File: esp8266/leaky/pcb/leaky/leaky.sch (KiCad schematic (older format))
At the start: 31 parts, among them J1 UART, J2 extra pins, Q1 BC327, SW1 sensing top, SW2 sensing bot, U1 DD0405MA, U2 ESP-12F

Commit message: leaky: Test routing
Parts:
- removed SW2: sensing bot, Connector_PinHeader_2.54mm:PinHeader_1x02_P2.54mm_Vertical, symbol Switch:SW_SPST
- SW1: value sensing top -> sensing loop
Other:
- moved on the sheet: C3, JP2, Q1, R1, R2, R3, SW1, TP3, TP4
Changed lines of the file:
@@
 L Transistor_BJT:BC327 Q1
 U 1 1 5F78C4AB
-P 2050 2350
-F 0 "Q1" H 2241 2304 50  0000 L CNN
-F 1 "BC327" H 2241 2395 50  0000 L CNN
-F 2 "Package_TO_SOT_THT:TO-92_Inline" H 2250 2275 50  0001 L CIN
-F 3 "http://www.onsemi.com/pub_link/Collateral/BC327-D.PDF" H 2050 2350 50  0001 L CNN
-	1    2050 2350
+P 1910 2640
+F 0 "Q1" H 2101 2594 50  0000 L CNN
+F 1 "BC327" H 2101 2685 50  0000 L CNN
+F 2 "Package_TO_SOT_THT:TO-92_Inline" H 2110 2565 50  0001 L CIN
+F 3 "http://www.onsemi.com/pub_link/Collateral/BC327-D.PDF" H 1910 2640 50  0001 L CNN
+	1    1910 2640
 	1    0    0    1
 $EndComp
@@
 L power:+3V3 #PWR0105
 U 1 1 5F78E830
-P 2150 2150
-F 0 "#PWR0105" H 2150 2000 50  0001 C CNN
-F 1 "+3V3" H 2165 2323 50  0000 C CNN
-F 2 "" H 2150 2150 50  0001 C CNN
-F 3 "" H 2150 2150 50  0001 C CNN
-	1    2150 2150
+P 2010 2440
+F 0 "#PWR0105" H 2010 2290 50  0001 C CNN
+F 1 "+3V3" H 2025 2613 50  0000 C CNN
+F 2 "" H 2010 2440 50  0001 C CNN
+F 3 "" H 2010 2440 50  0001 C CNN
+	1    2010 2440
 	1    0    0    -1
 $EndComp
@@
 L Device:R_Small R1
 U 1 1 5F78FD80
-P 1750 2350
-F 0 "R1" V 1650 2350 50  0000 C CNN
-F 1 "1k" V 1850 2350 50  0000 C CNN
-F 2 "Resistor_SMD:R_0805_2012Metric_Pad1.15x1.40mm_HandSolder" H 1750 2350 50  0001 C CNN
-F 3 "~" H 1750 2350 50  0001 C CNN
-	1    1750 2350
+P 1610 2640
+F 0 "R1" V 1510 2640 50  0000 C CNN
+F 1 "1k" V 1710 2640 50  0000 C CNN
+F 2 "Resistor_SMD:R_0805_2012Metric_Pad1.15x1.40mm_HandSolder" H 1610 2640 50  0001 C CNN
+F 3 "~" H 1610 2640 50  0001 C CNN
+	1    1610 2640
 	0    1    1    0
 $EndComp
@@
 L Switch:SW_SPST SW1
 U 1 1 5F792B65
-P 1100 2350
-F 0 "SW1" H 950 2450 50  0000 C CNN
-F 1 "sensing top" H 1150 2250 50  0000 C CNN
-F 2 "Connector_PinHeader_2.54mm:PinHeader_1x02_P2.54mm_Vertical" H 1100 2350 50  0001 C CNN
-F 3 "~" H 1100 2350 50  0001 C CNN
-	1    1100 2350
+P 1180 2640
+F 0 "SW1" H 1030 2740 50  0000 C CNN
+F 1 "sensing loop" H 1140 2540 50  0000 C CNN
+F 2 "Connector_PinHeader_2.54mm:PinHeader_1x02_P2.54mm_Vertical" H 1180 2640 50  0001 C CNN
+F 3 "~" H 1180 2640 50  0001 C CNN
+	1    1180 2640
 	-1   0    0    -1
 $EndComp
@@
 L power:GND #PWR01
 U 1 1 5F793765
-P 800 3080
-F 0 "#PWR01" H 800 2830 50  0001 C CNN
-F 1 "GND" H 805 2907 50  0000 C CNN
-F 2 "" H 800 3080 50  0001 C CNN
-F 3 "" H 800 3080 50  0001 C CNN
-	1    800  3080
+P 860 2820
+F 0 "#PWR01" H 860 2570 50  0001 C CNN
+F 1 "GND" H 865 2647 50  0000 C CNN
+F 2 "" H 860 2820 50  0001 C CNN
+F 3 "" H 860 2820 50  0001 C CNN
+	1    860  2820
 	1    0    0    -1
 $EndComp
@@
 L Device:R_Small R2
 U 1 1 5F7959A8
-P 2150 3000
-F 0 "R2" H 1950 3050 50  0000 L CNN
-F 1 "1k" H 1950 2950 50  0000 L CNN
-F 2 "Resistor_SMD:R_0805_2012Metric_Pad1.15x1.40mm_HandSolder" H 2150 3000 50  0001 C CNN
-F 3 "~" H 2150 3000 50  0001 C CNN
-	1    2150 3000
+P 2010 3290
+F 0 "R2" H 1810 3340 50  0000 L CNN
+F 1 "1k" H 1810 3240 50  0000 L CNN
+F 2 "Resistor_SMD:R_0805_2012Metric_Pad1.15x1.40mm_HandSolder" H 2010 3290 50  0001 C CNN
+F 3 "~" H 2010 3290 50  0001 C CNN
+	1    2010 3290
 	1    0    0    -1
 $EndComp
@@
 L power:GND #PWR02
 U 1 1 5F7965D3
-P 2150 3200
-F 0 "#PWR02" H 2150 2950 50  0001 C CNN
-F 1 "GND" H 2155 3027 50  0000 C CNN
-F 2 "" H 2150 3200 50  0001 C CNN
-F 3 "" H 2150 3200 50  0001 C CNN
-	1    2150 3200
-	1    0    0    -1
-$EndComp
-Wire Wire Line
-	2150 3200 2150 3150
+P 2010 3490
+F 0 "#PWR02" H 2010 3240 50  0001 C CNN
+F 1 "GND" H 2015 3317 50  0000 C CNN
+F 2 "" H 2010 3490 50  0001 C CNN
+F 3 "" H 2010 3490 50  0001 C CNN
+	1    2010 3490
+	1    0    0    -1
+$EndComp
+Wire Wire Line
+	2010 3490 2010 3440
 $Comp
 L Device:R_Small R3
 U 1 1 5F796B46
-P 2450 2850
-F 0 "R3" V 2350 2800 50  0000 L CNN
-F 1 "10k" V 2550 2800 50  0000 L CNN
-F 2 "Resistor_SMD:R_0805_2012Metric_Pad1.15x1.40mm_HandSolder" H 2450 2850 50  0001 C CNN
-F 3 "~" H 2450 2850 50  0001 C CNN
-	1    2450 2850
-	0    1    1    0
-$EndComp
-Wire Wire Line
-	2350 2850 2150 2850
-Connection ~ 2150 2850
-Wire Wire Line
-	2150 2850 2150 2900
+P 2310 3140
+F 0 "R3" V 2210 3090 50  0000 L CNN
+F 1 "10k" V 2410 3090 50  0000 L CNN
+F 2 "Resistor_SMD:R_0805_2012Metric_Pad1.15x1.40mm_HandSolder" H 2310 3140 50  0001 C CNN
+F 3 "~" H 2310 3140 50  0001 C CNN
+	1    2310 3140
+	0    1    1    0
+$EndComp
+Wire Wire Line
+	2210 3140 2010 3140
+Connection ~ 2010 3140
+Wire Wire Line
+	2010 3140 2010 3190
 $Comp
 L Device:C_Small C3
 U 1 1 5F797694
-P 2700 2950
-F 0 "C3" H 2850 2950 50  0000 C CNN
-F 1 "10uF" H 2850 2850 50  0000 C CNN
-F 2 "Capacitor_SMD:C_0805_2012Metric_Pad1.18x1.45mm_HandSolder" H 2700 2950 50  0001 C CNN
-F 3 "~" H 2700 2950 50  0001 C CNN
-	1    2700 2950
-	1    0    0    -1
-$EndComp
-Wire Wire Line
-	2550 2850 2700 2850
-Connection ~ 2150 3150
-Wire Wire Line
-	2150 3150 2150 3100
-Text GLabel 3050 2850 2    50   Input ~ 0
+P 2560 3240
+F 0 "C3" H 2710 3240 50  0000 C CNN
+F 1 "10uF" H 2710 3140 50  0000 C CNN
+F 2 "Capacitor_SMD:C_0805_2012Metric_Pad1.18x1.45mm_HandSolder" H 2560 3240 50  0001 C CNN
+F 3 "~" H 2560 3240 50  0001 C CNN
+	1    2560 3240
+	1    0    0    -1
+$EndComp
+Wire Wire Line
+	2410 3140 2560 3140
+Connection ~ 2010 3440
+Wire Wire Line
+	2010 3440 2010 3390
+Text GLabel 2910 3140 2    50   Input ~ 0
 EN
-Connection ~ 2700 2850
-Wire Wire Line
-	2700 3050 2700 3150
-Wire Wire Line
-	2700 2850 2900 2850
-Wire Wire Line
-	2700 3150 2150 3150
-Wire Wire Line
-	1300 2350 1450 2350
-Wire Wire Line
-	1450 2700 1300 2700
-Connection ~ 1450 2350
-Wire Wire Line
-	1450 2350 1650 2350
-Wire Wire Line
-	900  2350 800  2350
-Wire Wire Line
-	800  2350 800  2700
-Wire Wire Line
-	800  2700 900  2700
-Connection ~ 800  2700
+Connection ~ 2560 3140
+Wire Wire Line
+	2560 3340 2560 3440
+Wire Wire Line
+	2560 3140 2760 3140
+Wire Wire Line
+	2560 3440 2010 3440
 $Comp
 L power:+3V3 #PWR07
@@
 L Device:Jumper_NO_Small JP2
 U 1 1 5F7E84A9
-P 2700 2550
-F 0 "JP2" V 2700 2350 50  0000 L CNN
-F 1 "TURN_ON" V 2700 2600 50  0000 L CNN
-F 2 "Connector_PinHeader_2.54mm:PinHeader_1x02_P2.54mm_Vertical" H 2700 2550 50  0001 C CNN
-F 3 "~" H 2700 2550 50  0001 C CNN
-	1    2700 2550
+P 2560 2840
+F 0 "JP2" V 2560 2640 50  0000 L CNN
+F 1 "TURN_ON" V 2560 2890 50  0000 L CNN
+F 2 "Connector_PinHeader_2.54mm:PinHeader_1x02_P2.54mm_Vertical" H 2560 2840 50  0001 C CNN
+F 3 "~" H 2560 2840 50  0001 C CNN
+	1    2560 2840
 	0    1    1    0
 $EndComp
@@
 $EndComp
 Wire Wire Line
-	2700 2650 2150 2650
-Wire Wire Line
-	2150 2650 2150 2550
-Wire Wire Line
-	2150 2650 2150 2750
-Connection ~ 2150 2650
-Wire Wire Line
-	2700 2150 2700 2450
+	2560 2940 2010 2940
+Wire Wire Line
+	2010 2940 2010 2840
+Wire Wire Line
+	2010 2940 2010 3040
+Connection ~ 2010 2940
+Wire Wire Line
+	2560 2440 2560 2740
 $Comp
 L power:+3V3 #PWR011
 U 1 1 5F7EE7D8
-P 2700 2150
-F 0 "#PWR011" H 2700 2000 50  0001 C CNN
-F 1 "+3V3" H 2715 2323 50  0000 C CNN
-F 2 "" H 2700 2150 50  0001 C CNN
-F 3 "" H 2700 2150 50  0001 C CNN
-	1    2700 2150
+P 2560 2440
+F 0 "#PWR011" H 2560 2290 50  0001 C CNN
+F 1 "+3V3" H 2575 2613 50  0000 C CNN
+F 2 "" H 2560 2440 50  0001 C CNN
+F 3 "" H 2560 2440 50  0001 C CNN
+	1    2560 2440
 	1    0    0    -1
 $EndComp
@@
 L Connector:TestPoint TP4
 U 1 1 5F7F5357
-P 2900 2850
-F 0 "TP4" H 2950 3000 50  0000 L CNN
-F 1 "TestPoint" H 2958 2877 50  0001 L CNN
-F 2 "TestPoint:TestPoint_Pad_D1.0mm" H 3100 2850 50  0001 C CNN
-F 3 "~" H 3100 2850 50  0001 C CNN
-	1    2900 2850
-	1    0    0    -1
-$EndComp
-Connection ~ 2900 2850
-Wire Wire Line
-	2900 2850 3050 2850
+P 2760 3140
+F 0 "TP4" H 2810 3290 50  0000 L CNN
+F 1 "TestPoint" H 2818 3167 50  0001 L CNN
+F 2 "TestPoint:TestPoint_Pad_D1.0mm" H 2960 3140 50  0001 C CNN
+F 3 "~" H 2960 3140 50  0001 C CNN
+	1    2760 3140
+	1    0    0    -1
+$EndComp
+Connection ~ 2760 3140
+Wire Wire Line
+	2760 3140 2910 3140
 $Comp
 L Connector:TestPoint TP3
 U 1 1 5F7F5A10
-P 2150 2750
-F 0 "TP3" V 2150 2950 50  0000 L CNN
-F 1 "TestPoint" H 2208 2777 50  0001 L CNN
-F 2 "TestPoint:TestPoint_Pad_D1.0mm" H 2350 2750 50  0001 C CNN
-F 3 "~" H 2350 2750 50  0001 C CNN
-	1    2150 2750
+P 2010 3040
+F 0 "TP3" V 2010 3240 50  0000 L CNN
+F 1 "TestPoint" H 2068 3067 50  0001 L CNN
+F 2 "TestPoint:TestPoint_Pad_D1.0mm" H 2210 3040 50  0001 C CNN
+F 3 "~" H 2210 3040 50  0001 C CNN
+	1    2010 3040
 	0    -1   -1   0
 $EndComp
-Connection ~ 2150 2750
-Wire Wire Line
-	2150 2750 2150 2850
+Connection ~ 2010 3040
+Wire Wire Line
+	2010 3040 2010 3140
 Wire Wire Line
 	1800 950  1800 1000
@@
 Text Notes 5160 1980 0    50   ~ 0
 ESP-12F
-Text Notes 650  2100 0    50   ~ 0
+Text Notes 720  2310 0    50   ~ 0
 Water sensing circuit\n
 Text Notes 3370 3340 0    50   ~ 0
@@
 Text GLabel 8170 5230 0    50   Input ~ 0
 IO13
-Wire Wire Line
-	1450 2350 1450 2700
 $Comp
 L Mechanical:MountingHole H1
@@
 Text Notes 780  4080 0    50   ~ 0
 Mounting holes
-Wire Wire Line
-	800  2700 800  3080
 $Comp
 L _mysyms:ESP-12F U2
@@
 Text Notes 5120 4400 0    50   ~ 0
 VBUS voltage has to be 3V3, not 5V!\nIf you provide power through VBUS, remove batteries first.\nTo flash program: \n  1. Short jumper PROG\n  2. Connect UART\n  3. Short jumper TURN_ON\n
-$Comp
-L Switch:SW_SPST SW2
-U 1 1 5F79B9DC
-P 1100 2700
-F 0 "SW2" H 950 2800 50  0000 C CNN
-F 1 "sensing bot" H 1150 2600 50  0000 C CNN
-F 2 "Connector_PinHeader_2.54mm:PinHeader_1x02_P2.54mm_Vertical" H 1100 2700 50  0001 C CNN
-F 3 "~" H 1100 2700 50  0001 C CNN
-	1    1100 2700
-	-1   0    0    -1
-$EndComp
+Wire Wire Line
+	1510 2640 1380 2640
+Wire Wire Line
+	980  2640 860  2640
+Wire Wire Line
+	860  2640 860  2820
 $EndSCHEMATC

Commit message: leaky: Start working on bat footprint
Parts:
- BT1: footprint Battery:BatteryHolder_Keystone_2462_2xAA -> _my:BatteryHolder_Keystone_2462_2xAA
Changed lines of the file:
@@
 F 0 "BT1" H 1000 1300 50  0000 L CNN
 F 1 "2xAA" H 950 1200 50  0000 L CNN
-F 2 "Battery:BatteryHolder_Keystone_2462_2xAA" V 1300 1260 50  0001 C CNN
+F 2 "_my:BatteryHolder_Keystone_2462_2xAA" V 1300 1260 50  0001 C CNN
 F 3 "~" V 1300 1260 50  0001 C CNN
 	1    1300 1200

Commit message: leaky: Add bat footprint
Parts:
- H1, H2, H3, H4: footprint MountingHole:MountingHole_3.2mm_M3 -> _my:MountingHole_3.2mm_M3
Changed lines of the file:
@@
 $EndDescr
-$Comp
-L Device:Battery BT1
-U 1 1 5F780761
-P 1300 1200
-F 0 "BT1" H 1000 1300 50  0000 L CNN
-F 1 "2xAA" H 950 1200 50  0000 L CNN
-F 2 "_my:BatteryHolder_Keystone_2462_2xAA" V 1300 1260 50  0001 C CNN
-F 3 "~" V 1300 1260 50  0001 C CNN
-	1    1300 1200
-	1    0    0    -1
-$EndComp
 $Comp
 L power:GND #PWR0101
@@
 F 0 "H1" H 940 4380 50  0000 L CNN
 F 1 "MountingHole" H 940 4335 50  0001 L CNN
-F 2 "MountingHole:MountingHole_3.2mm_M3" H 840 4380 50  0001 C CNN
+F 2 "_my:MountingHole_3.2mm_M3" H 840 4380 50  0001 C CNN
 F 3 "~" H 840 4380 50  0001 C CNN
 	1    840  4380
@@
 F 0 "H2" H 940 4630 50  0000 L CNN
 F 1 "MountingHole" H 940 4585 50  0001 L CNN
-F 2 "MountingHole:MountingHole_3.2mm_M3" H 840 4630 50  0001 C CNN
+F 2 "_my:MountingHole_3.2mm_M3" H 840 4630 50  0001 C CNN
 F 3 "~" H 840 4630 50  0001 C CNN
 	1    840  4630
@@
 F 0 "H3" H 1300 4390 50  0000 L CNN
 F 1 "MountingHole" H 1300 4345 50  0001 L CNN
-F 2 "MountingHole:MountingHole_3.2mm_M3" H 1200 4390 50  0001 C CNN
+F 2 "_my:MountingHole_3.2mm_M3" H 1200 4390 50  0001 C CNN
 F 3 "~" H 1200 4390 50  0001 C CNN
 	1    1200 4390
@@
 F 0 "H4" H 1300 4640 50  0000 L CNN
 F 1 "MountingHole" H 1300 4595 50  0001 L CNN
-F 2 "MountingHole:MountingHole_3.2mm_M3" H 1200 4640 50  0001 C CNN
+F 2 "_my:MountingHole_3.2mm_M3" H 1200 4640 50  0001 C CNN
 F 3 "~" H 1200 4640 50  0001 C CNN
 	1    1200 4640
@@
 Wire Wire Line
 	860  2640 860  2820
+$Comp
+L Device:Battery BT1
+U 1 1 5F780761
+P 1300 1200
+F 0 "BT1" H 1000 1300 50  0000 L CNN
+F 1 "2xAA" H 950 1200 50  0000 L CNN
+F 2 "_my:BatteryHolder_Keystone_2462_2xAA" V 1300 1260 50  0001 C CNN
+F 3 "~" V 1300 1260 50  0001 C CNN
+	1    1300 1200
+	1    0    0    -1
+$EndComp
 $EndSCHEMATC

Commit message: leaky: Adjust silk screen
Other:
- note added: "Extra pins"
- note removed: "Extra unused pins"
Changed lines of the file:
@@
 Programming header
 Text Notes 7730 4700 0    50   ~ 0
-Extra unused pins
+Extra pins
 Text GLabel 7150 2800 2    50   Input ~ 0
 BUZZER

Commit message: leaky: Adjust cap
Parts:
- C1: footprint Capacitor_THT:CP_Radial_D10.0mm_P5.00mm -> _my:CP_Radial_D10.0mm_P5.00mm
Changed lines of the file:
@@
 F 0 "C1" H 3050 1400 50  0000 C CNN
 F 1 "2200uF" H 3050 1300 50  0000 C CNN
-F 2 "Capacitor_THT:CP_Radial_D10.0mm_P5.00mm" H 3050 1100 50  0001 C CNN
+F 2 "_my:CP_Radial_D10.0mm_P5.00mm" H 3050 1100 50  0001 C CNN
 F 3 "~" H 3050 1100 50  0001 C CNN
 	1    3050 1100

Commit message: leaky: Update schema
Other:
- note added: "Custom sensor can be connected to SW1"
- note added: "Extra pins for custom use"
- note added: "Leaky"
- note added: "v1.0"
- note removed: "Extra pins"
- moved on the sheet: BZ1, C3, C4, H1, H2, H3, H4, J1, J2, JP1, JP2, Q1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

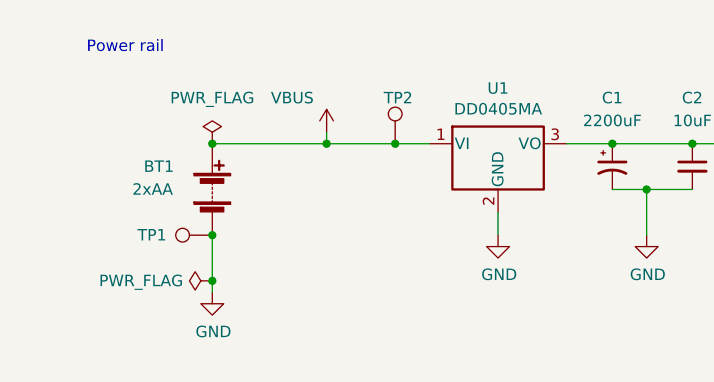
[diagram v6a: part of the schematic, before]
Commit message: leaky: Position test points
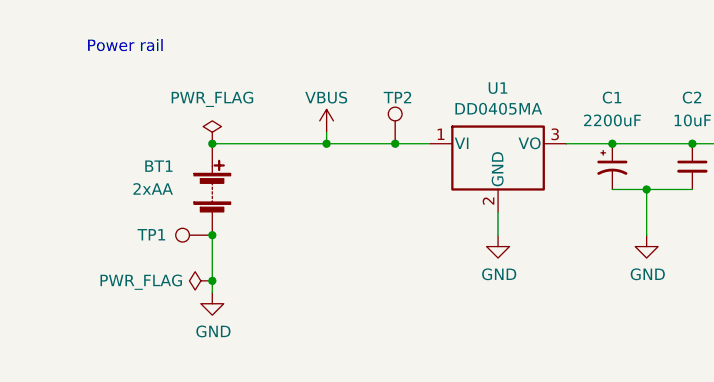
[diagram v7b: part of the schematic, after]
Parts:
- Q1: footprint Package_TO_SOT_THT:TO-92_Inline -> _my:TO-92_Inline
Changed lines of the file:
@@
 F 0 "Q1" H 2101 3144 50  0000 L CNN
 F 1 "BC327" H 2101 3235 50  0000 L CNN
-F 2 "Package_TO_SOT_THT:TO-92_Inline" H 2110 3115 50  0001 L CIN
+F 2 "_my:TO-92_Inline" H 2110 3115 50  0001 L CIN
 F 3 "http://www.onsemi.com/pub_link/Collateral/BC327-D.PDF" H 1910 3190 50  0001 L CNN
 	1    1910 3190
@@
 P 1800 950
 F 0 "#PWR03" H 1800 800 50  0001 C CNN
-F 1 "VBUS" H 1650 1100 50  0000 C CNN
+F 1 "VBUS" H 1800 1100 50  0000 C CNN
 F 2 "" H 1800 950 50  0001 C CNN
 F 3 "" H 1800 950 50  0001 C CNN

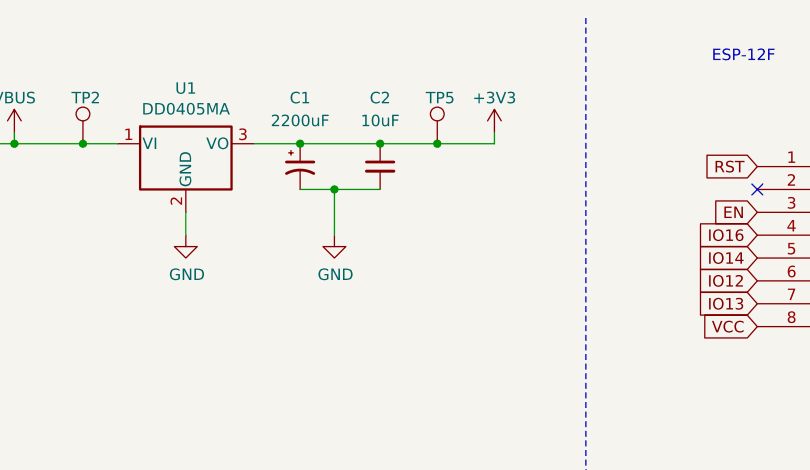
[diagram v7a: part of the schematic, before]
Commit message: leaky: Adjust PCB
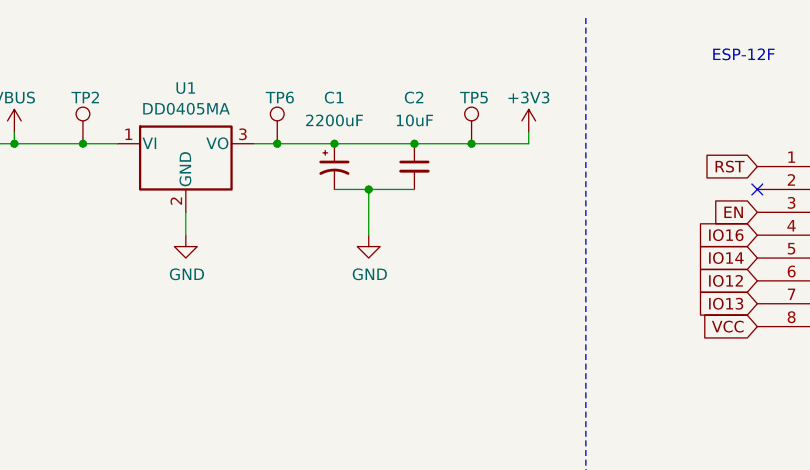
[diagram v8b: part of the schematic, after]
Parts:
- added TP6: TestPoint, TestPoint:TestPoint_Pad_D1.0mm, symbol Connector:TestPoint
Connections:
- net +3V3: now also TP6.1
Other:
- moved on the sheet: C1, C2, TP5
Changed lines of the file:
@@
 L Device:CP1_Small C1
 U 1 1 5F782867
-P 3050 1100
-F 0 "C1" H 3050 1400 50  0000 C CNN
-F 1 "2200uF" H 3050 1300 50  0000 C CNN
-F 2 "_my:CP_Radial_D10.0mm_P5.00mm" H 3050 1100 50  0001 C CNN
-F 3 "~" H 3050 1100 50  0001 C CNN
-	1    3050 1100
+P 3200 1100
+F 0 "C1" H 3200 1400 50  0000 C CNN
+F 1 "2200uF" H 3200 1300 50  0000 C CNN
+F 2 "_my:CP_Radial_D10.0mm_P5.00mm" H 3200 1100 50  0001 C CNN
+F 3 "~" H 3200 1100 50  0001 C CNN
+	1    3200 1100
 	1    0    0    -1
 $EndComp
@@
 L Device:C_Small C2
 U 1 1 5F784ED8
-P 3400 1100
-F 0 "C2" H 3400 1400 50  0000 C CNN
-F 1 "10uF" H 3400 1300 50  0000 C CNN
-F 2 "Capacitor_SMD:C_0805_2012Metric_Pad1.18x1.45mm_HandSolder" H 3400 1100 50  0001 C CNN
-F 3 "~" H 3400 1100 50  0001 C CNN
-	1    3400 1100
-	1    0    0    -1
-$EndComp
-Wire Wire Line
-	2850 1000 3050 1000
+P 3550 1100
+F 0 "C2" H 3550 1400 50  0000 C CNN
+F 1 "10uF" H 3550 1300 50  0000 C CNN
+F 2 "Capacitor_SMD:C_0805_2012Metric_Pad1.18x1.45mm_HandSolder" H 3550 1100 50  0001 C CNN
+F 3 "~" H 3550 1100 50  0001 C CNN
+	1    3550 1100
+	1    0    0    -1
+$EndComp
 $Comp
 L power:GND #PWR0103
 U 1 1 5F78959B
-P 3200 1400
-F 0 "#PWR0103" H 3200 1150 50  0001 C CNN
-F 1 "GND" H 3205 1227 50  0000 C CNN
-F 2 "" H 3200 1400 50  0001 C CNN
-F 3 "" H 3200 1400 50  0001 C CNN
-	1    3200 1400
-	1    0    0    -1
-$EndComp
-Wire Wire Line
-	3050 1200 3200 1200
-Wire Wire Line
-	3050 1000 3400 1000
-Connection ~ 3050 1000
-Wire Wire Line
-	3200 1200 3200 1400
-Connection ~ 3200 1200
-Wire Wire Line
-	3200 1200 3400 1200
-Wire Wire Line
-	3400 1000 3650 1000
-Connection ~ 3400 1000
+P 3350 1400
+F 0 "#PWR0103" H 3350 1150 50  0001 C CNN
+F 1 "GND" H 3355 1227 50  0000 C CNN
+F 2 "" H 3350 1400 50  0001 C CNN
+F 3 "" H 3350 1400 50  0001 C CNN
+	1    3350 1400
+	1    0    0    -1
+$EndComp
+Wire Wire Line
+	3200 1200 3350 1200
+Wire Wire Line
+	3200 1000 3550 1000
+Connection ~ 3200 1000
+Wire Wire Line
+	3350 1200 3350 1400
+Connection ~ 3350 1200
+Wire Wire Line
+	3350 1200 3550 1200
+Wire Wire Line
+	3550 1000 3800 1000
+Connection ~ 3550 1000
 $Comp
 L power:PWR_FLAG #FLG02
@@
 L power:+3V3 #PWR0104
 U 1 1 5F78E3C2
-P 3900 950
-F 0 "#PWR0104" H 3900 800 50  0001 C CNN
-F 1 "+3V3" H 3900 1100 50  0000 C CNN
-F 2 "" H 3900 950 50  0001 C CNN
-F 3 "" H 3900 950 50  0001 C CNN
-	1    3900 950
+P 4050 950
+F 0 "#PWR0104" H 4050 800 50  0001 C CNN
+F 1 "+3V3" H 4050 1100 50  0000 C CNN
+F 2 "" H 4050 950 50  0001 C CNN
+F 3 "" H 4050 950 50  0001 C CNN
+	1    4050 950
 	1    0    0    -1
 $EndComp
@@
 	2100 1000 2250 1000
 Wire Wire Line
-	3900 950  3900 1000
-Wire Wire Line
-	3900 1000 3650 1000
-Connection ~ 3650 1000
+	4050 950  4050 1000
+Wire Wire Line
+	4050 1000 3800 1000
+Connection ~ 3800 1000
 $Comp
 L Connector:TestPoint TP1
@@
 L Connector:TestPoint TP5
 U 1 1 5F7EFD59
-P 3650 1000
-F 0 "TP5" H 3600 1200 50  0000 L CNN
-F 1 "TestPoint" H 3708 1027 50  0001 L CNN
-F 2 "TestPoint:TestPoint_Pad_D1.0mm" H 3850 1000 50  0001 C CNN
-F 3 "~" H 3850 1000 50  0001 C CNN
-	1    3650 1000
+P 3800 1000
+F 0 "TP5" H 3750 1200 50  0000 L CNN
+F 1 "TestPoint" H 3858 1027 50  0001 L CNN
+F 2 "TestPoint:TestPoint_Pad_D1.0mm" H 4000 1000 50  0001 C CNN
+F 3 "~" H 4000 1000 50  0001 C CNN
+	1    3800 1000
 	1    0    0    -1
 $EndComp
@@
 Text Notes 10600 7650 0    59   ~ 0
 v1.0
+$Comp
+L Connector:TestPoint TP6
+U 1 1 5FB801A3
+P 2950 1000
+F 0 "TP6" H 2900 1200 50  0000 L CNN
+F 1 "TestPoint" H 3008 1027 50  0001 L CNN
+F 2 "TestPoint:TestPoint_Pad_D1.0mm" H 3150 1000 50  0001 C CNN
+F 3 "~" H 3150 1000 50  0001 C CNN
+	1    2950 1000
+	1    0    0    -1
+$EndComp
+Wire Wire Line
+	2850 1000 2950 1000
+Connection ~ 2950 1000
+Wire Wire Line
+	2950 1000 3200 1000
 $EndSCHEMATC
